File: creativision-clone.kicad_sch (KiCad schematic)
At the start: 71 parts, among them J1 Conn_01x10_Socket, J2 Conn_01x10_Socket, SW1 Reset, U1 AS6C62256-DIP, U100 74HCT574, U101 74HCT574, U102 74HCT574, U12 74LS32, U15 74LS139, U18 AS6C62256-DIP, U2 6502, U20 27256, U21 6821, U22 SN76489AN, U3 TMS9918A, U99 74HCT04, X1 2MHz

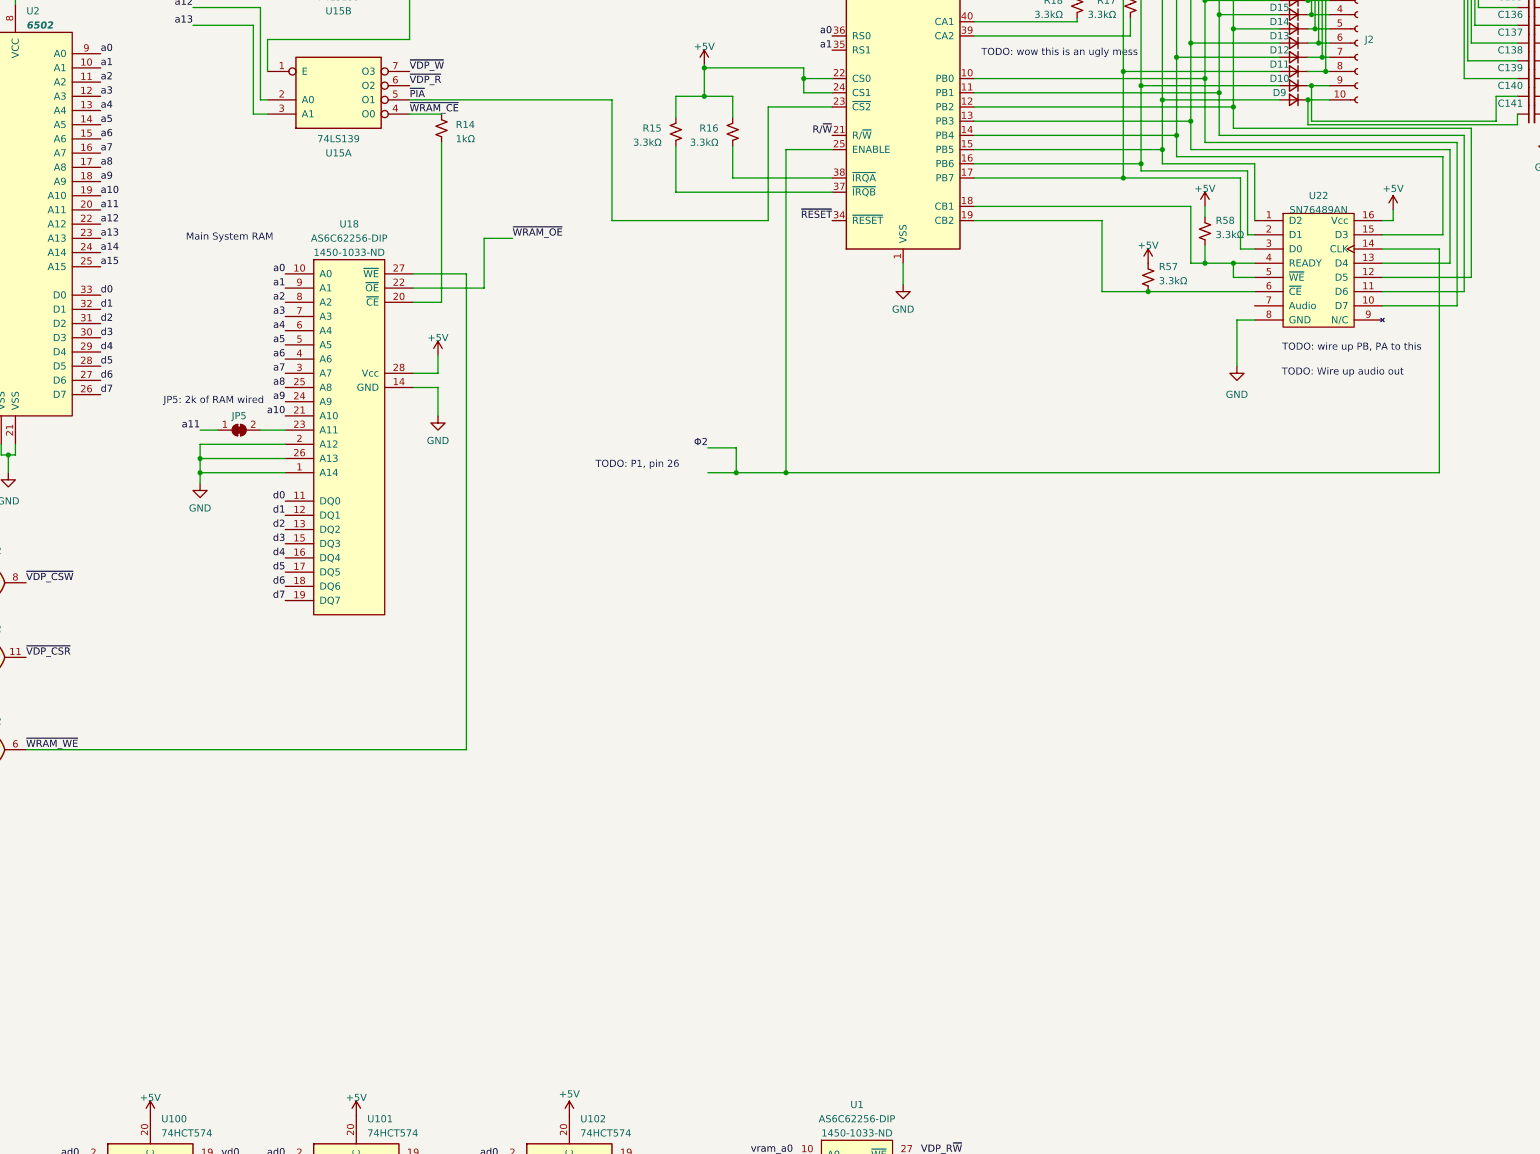
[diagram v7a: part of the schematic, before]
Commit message: Cartridge filled out except pin 30
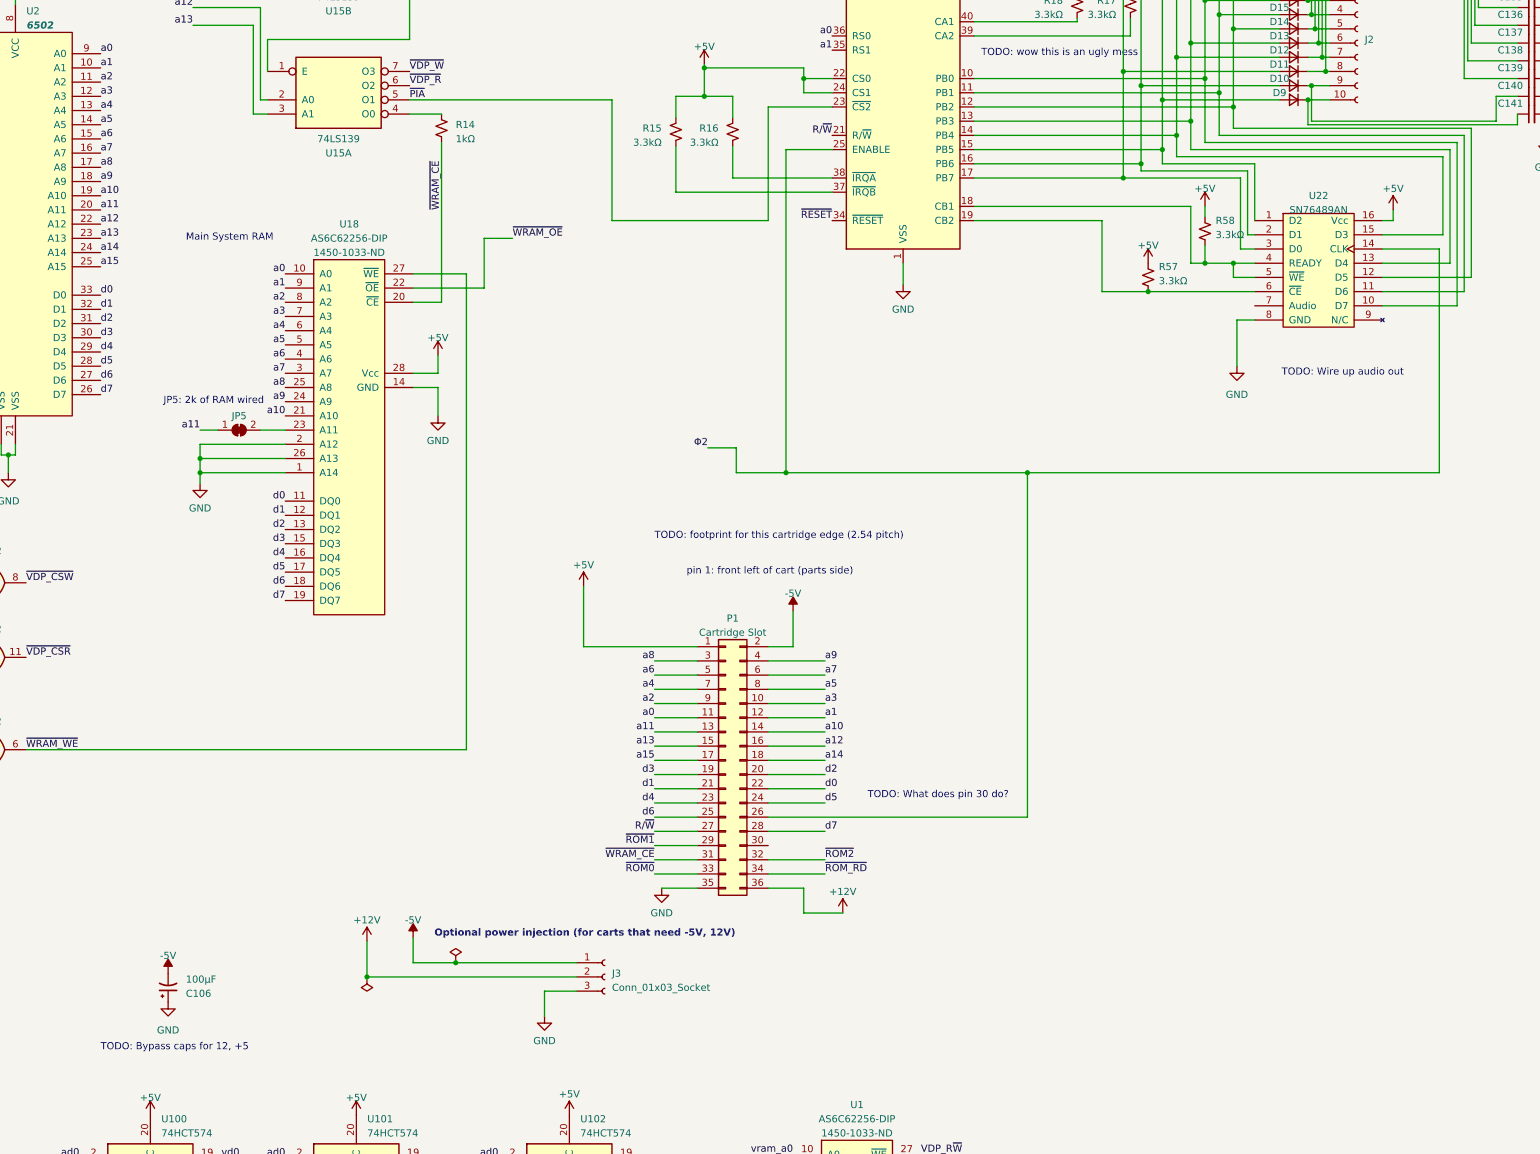
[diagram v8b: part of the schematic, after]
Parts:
- added C106: 100µF, symbol Device:C_Polarized_Small_US
- added J3: Conn_01x03_Socket, symbol Connector:Conn_01x03_Socket
- added P1: Cartridge Slot, symbol Connector_Generic:Conn_02x18_Odd_Even
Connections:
- net +5V: now also P1.1 (Pin_1)
- net GND: now also C106.1, J3.3 (Pin_3), P1.35 (Pin_35)
- net R/~{W}: now also P1.27 (Pin_27)
- net a0: now also P1.11 (Pin_11)
- net a1: now also P1.12 (Pin_12)
- net a10: now also P1.14 (Pin_14)
- net a11: now also P1.13 (Pin_13)
- net a12: now also P1.16 (Pin_16)
- net a13: now also P1.15 (Pin_15)
- net a14: now also P1.18 (Pin_18)
- net a15: now also P1.17 (Pin_17)
- net a2: now also P1.9 (Pin_9)
- net a3: now also P1.10 (Pin_10)
- net a4: now also P1.7 (Pin_7)
- net a5: now also P1.8 (Pin_8)
- net a6: now also P1.5 (Pin_5)
- net a7: now also P1.6 (Pin_6)
- net a8: now also P1.3 (Pin_3)
- net a9: now also P1.4 (Pin_4)
- net d0: now also P1.22 (Pin_22)
- net d1: now also P1.21 (Pin_21)
- net d2: now also P1.20 (Pin_20)
- net d3: now also P1.19 (Pin_19)
- net d4: now also P1.23 (Pin_23)
- net d5: now also P1.24 (Pin_24)
- net d6: now also P1.25 (Pin_25)
- net d7: now also P1.28 (Pin_28)
- net ~{ROM0}: now also P1.33 (Pin_33)
- net ~{ROM1}: now also P1.29 (Pin_29)
- net ~{ROM2}: now also P1.32 (Pin_32)
- net ~{ROM_RD}: now also P1.34 (Pin_34)
- net ~{WRAM_CE}: now also R14.2, U18.20 (~{CE}), P1.31 (Pin_31); no longer R14.1, U15.4 (O0)
- net Φ2: now also P1.26 (Pin_26)
- new net: R14.1, U15.4 (O0)
- new net +12V: J3.2 (Pin_2), P1.36 (Pin_36)
- new net -5V: C106.2, J3.1 (Pin_1), P1.2 (Pin_2)
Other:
- note added: "Optional power injection (for carts that need -5V, 12V)"
- note added: "TODO: Bypass caps for 12, +5"
- note added: "TODO: What does pin 30 do?"
- note added: "TODO: footprint for this cartridge edge (2.54 pitch)"
- note added: "pin 1: front left of cart (parts side)"
- note removed: "TODO: P1, pin 26"
- note removed: "TODO: wire up PB, PA to this"
